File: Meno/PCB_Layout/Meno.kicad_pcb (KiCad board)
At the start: 2 copper layers, 68.5 x 53.3 mm, 49 parts, among them J1 5077CR-16SMC2, J2 AVR-ISP-6, J3 18742, J4 Conn_02x19_Female, J5 Conn_02x12_Female, J6 Conn_02x15_Female, Q1 IRLML6402, SW1 B3FS-1050P, U1 ATmega2560-16AUR, U2 FT232RL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

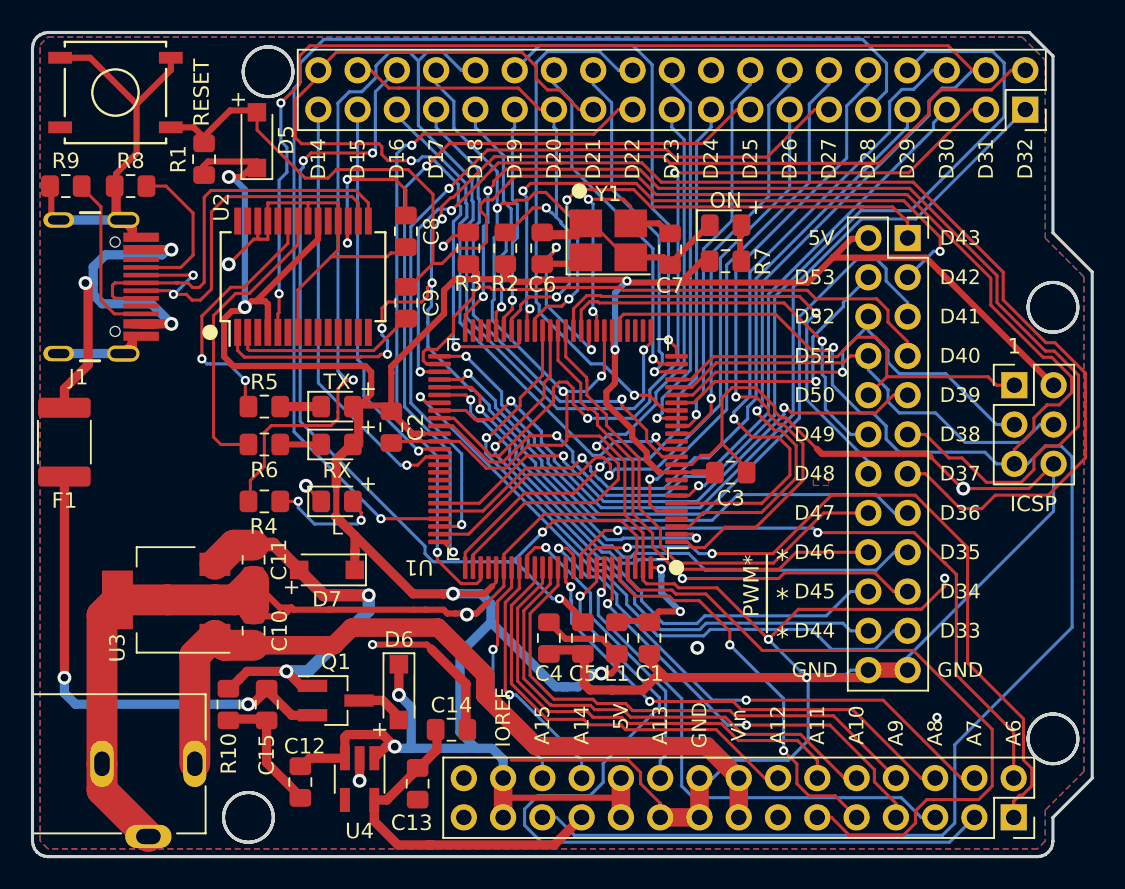
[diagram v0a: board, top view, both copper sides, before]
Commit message: ピンヘッダ/ソケットの位置を修正
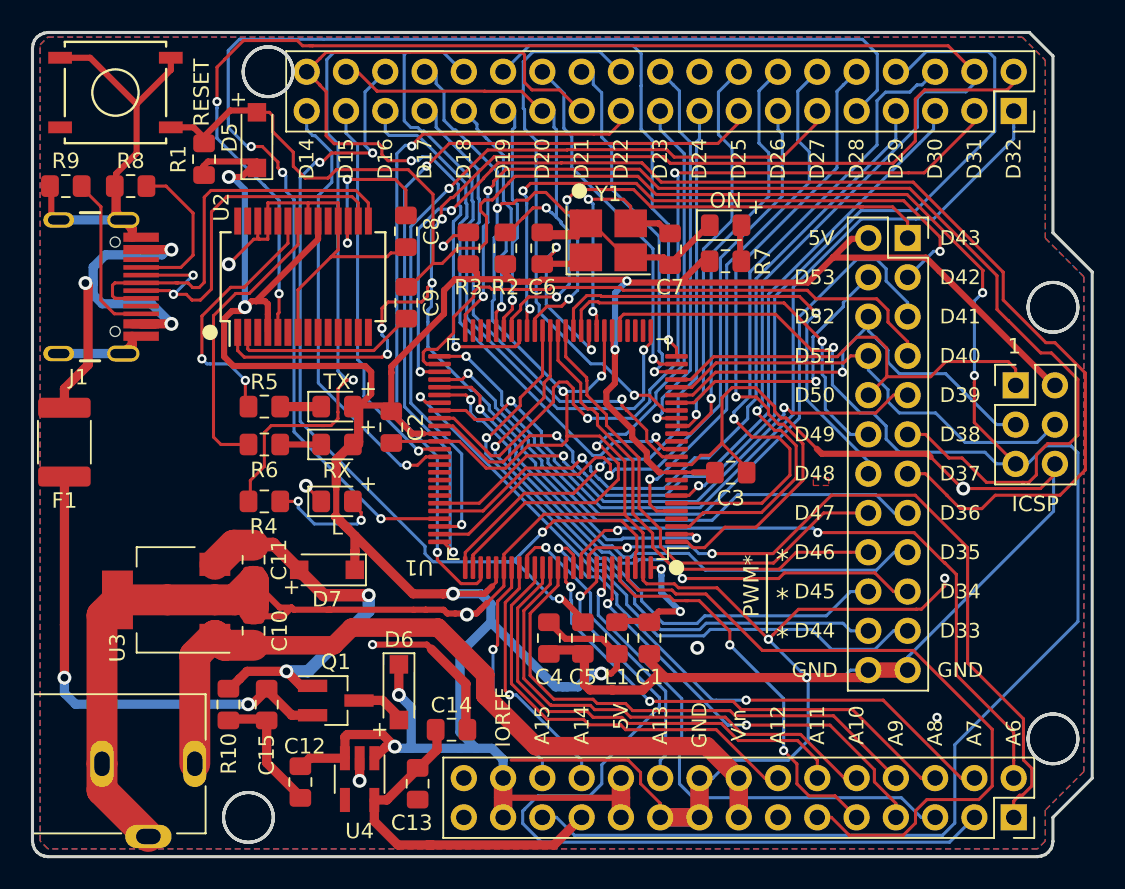
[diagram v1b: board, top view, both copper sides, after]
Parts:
- moved J4 0.76 mm to (177.7, 80.1)
- moved J2 0.09 mm to (177.8, 97.9)
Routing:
- net D28: track 78.4 -> 85.6 mm, vias 1 -> 3
- net D1: track 107.9 -> 114.7 mm
- net D13: track 80.5 -> 83.8 mm
- net GND: track 361.5 -> 364.6 mm
- net RST: track 180.6 -> 178.3 mm, vias 1 -> 3
- net D16: track 34.4 -> 36.1 mm
- net D50: track 27.0 -> 28.5 mm
- net D9: track 34.8 -> 36.0 mm
- net D0: track 94.8 -> 95.9 mm
- net D14: track 27.9 -> 29.0 mm
- net D30: track 51.5 -> 52.4 mm
- net D21: track 57.1 -> 56.2 mm
- net D12: track 29.6 -> 30.4 mm
- net D38: track 72.7 -> 73.4 mm
- net AREF: track 64.3 -> 63.8 mm
